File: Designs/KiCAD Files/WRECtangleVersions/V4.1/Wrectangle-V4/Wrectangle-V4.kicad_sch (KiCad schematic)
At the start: 67 parts, among them J10 xBee-Antenna1, J2 USB_C_Receptacle_USB2.0_16P, J3 AnalogIn-Terminal3, J4 AnalogIn-Terminal2, J5 AnalogIn-Terminal1, J6 AnalogIn-Terminal0, J7 GPS-Antenna, J8 Micro_SD_Card, U1 STM32F405RGTx, U10 FT232RL, U11 BME280, U2 BNO085_C5189642, U3 MAX-M10S-00B, U4 H3LIS331DLTR, U9 XBP9X-DMUS-001

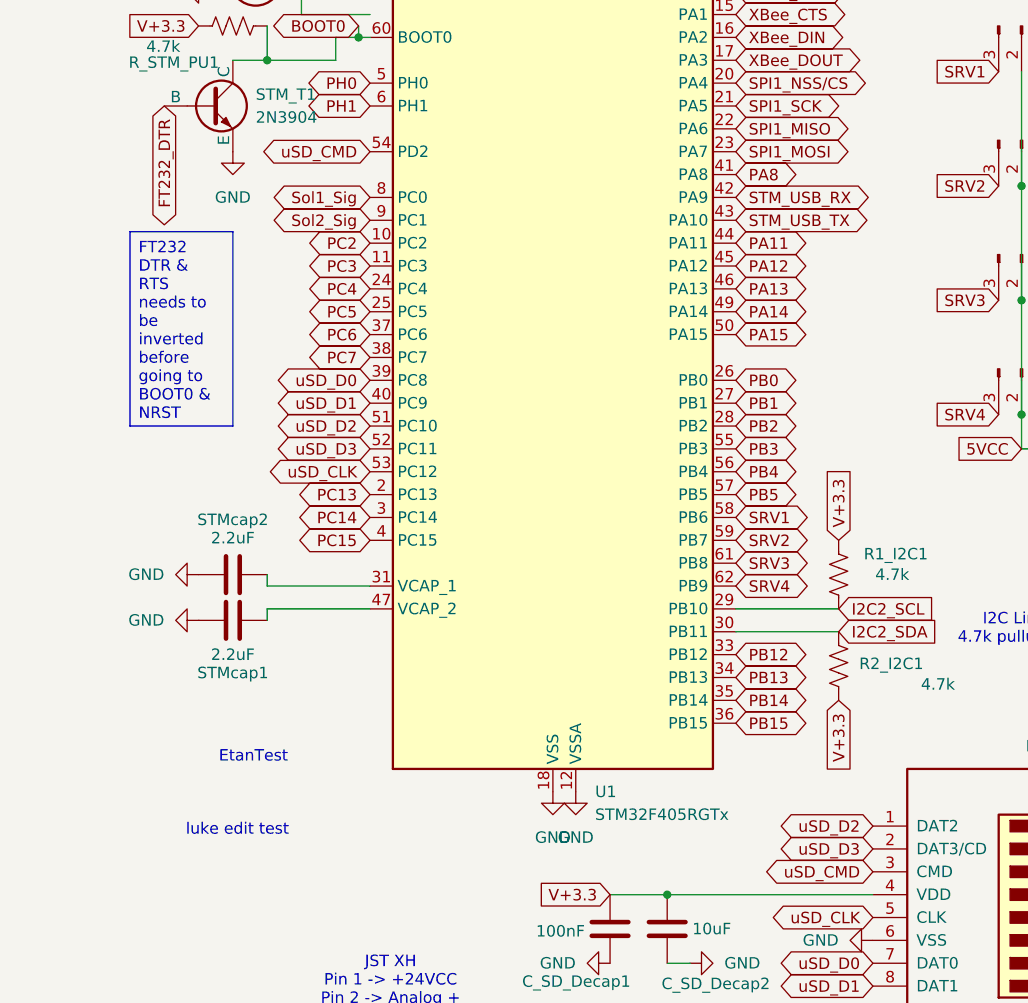
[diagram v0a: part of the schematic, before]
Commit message: made some minor fixes to pins
Added DRDY to ADC
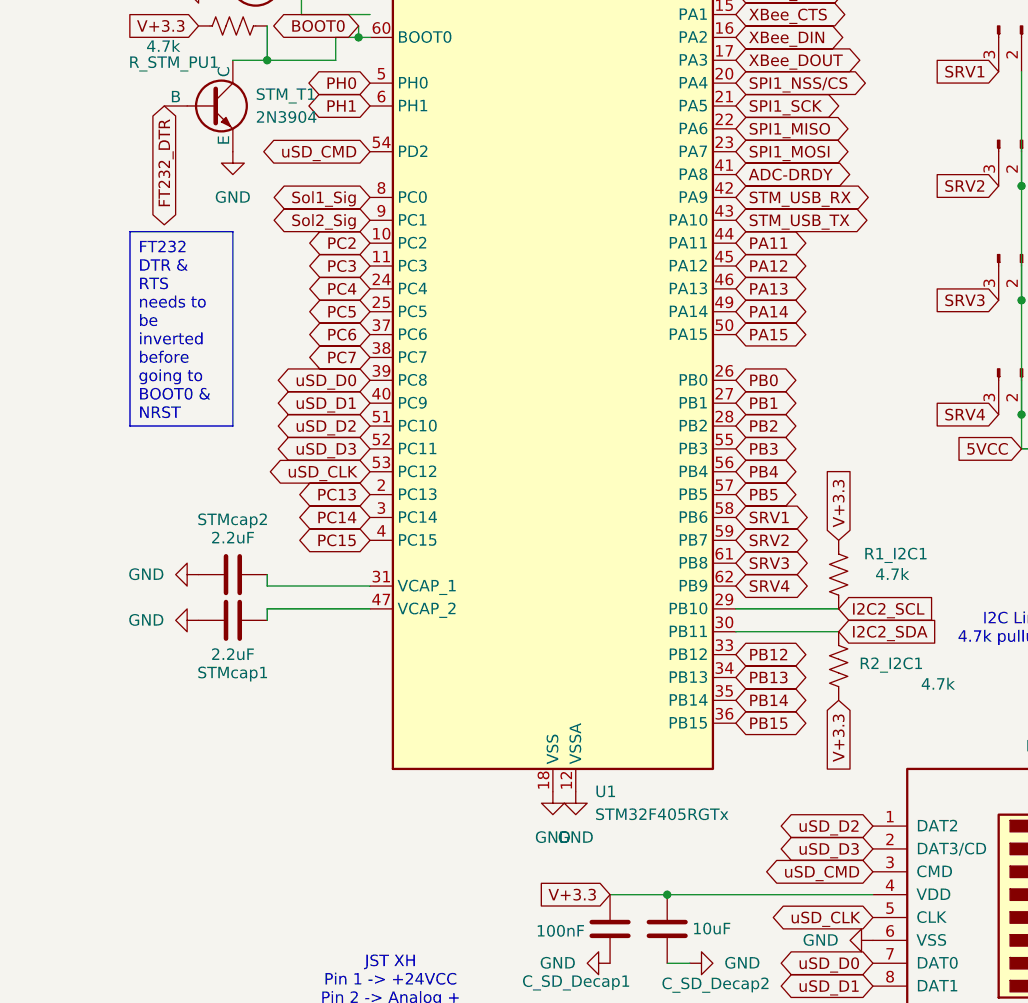
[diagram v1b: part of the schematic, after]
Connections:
- net PA8 renamed ADC-DRDY
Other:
- note removed: "EtanTest"
- note removed: "luke edit test"
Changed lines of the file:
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@@
 	(generator_version "9.0")
 	(paper "A4")
-	(text "EtanTest"
-		(exclude_from_sim no)
-		(at 26.416 121.92 0)
-		(effects
-			(font
-				(size 1.27 1.27)
-			)
-		)
-	)
 	(text "I2C Lines with \n4.7k pullup resistors"
 		(exclude_from_sim no)
@@
 		)
 	)
-	(text "luke edit test"
-		(exclude_from_sim no)
-		(at 24.638 130.048 0)
-		(effects
-			(font
-				(size 1.27 1.27)
-			)
-		)
-	)
 	(text "SDO to GND\nfor default\nI2C address"
 		(exclude_from_sim no)
@@
 		)
 	)
-	(global_label "PA8"
+	(global_label "ADC-DRDY"
 		(shape bidirectional)
 		(at 80.01 57.15 0)
@@
 		)
 		(property "Intersheetrefs" "${INTERSHEET_REFS}"
-			(at 87.6746 57.15 0)
+			(at 94.2061 57.15 0)
 			(effects
 				(font
